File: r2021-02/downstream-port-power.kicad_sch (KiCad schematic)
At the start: 33 parts, among them J4 USB_A (female down), J5 USB_A_Stacked, J6 USB_A_Stacked, J7 USB_A_Stacked, U10 APL3511C, U11 NUP4202, U12 NUP4202, U13 NUP4202, U14 NUP4202, U15 NUP4202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

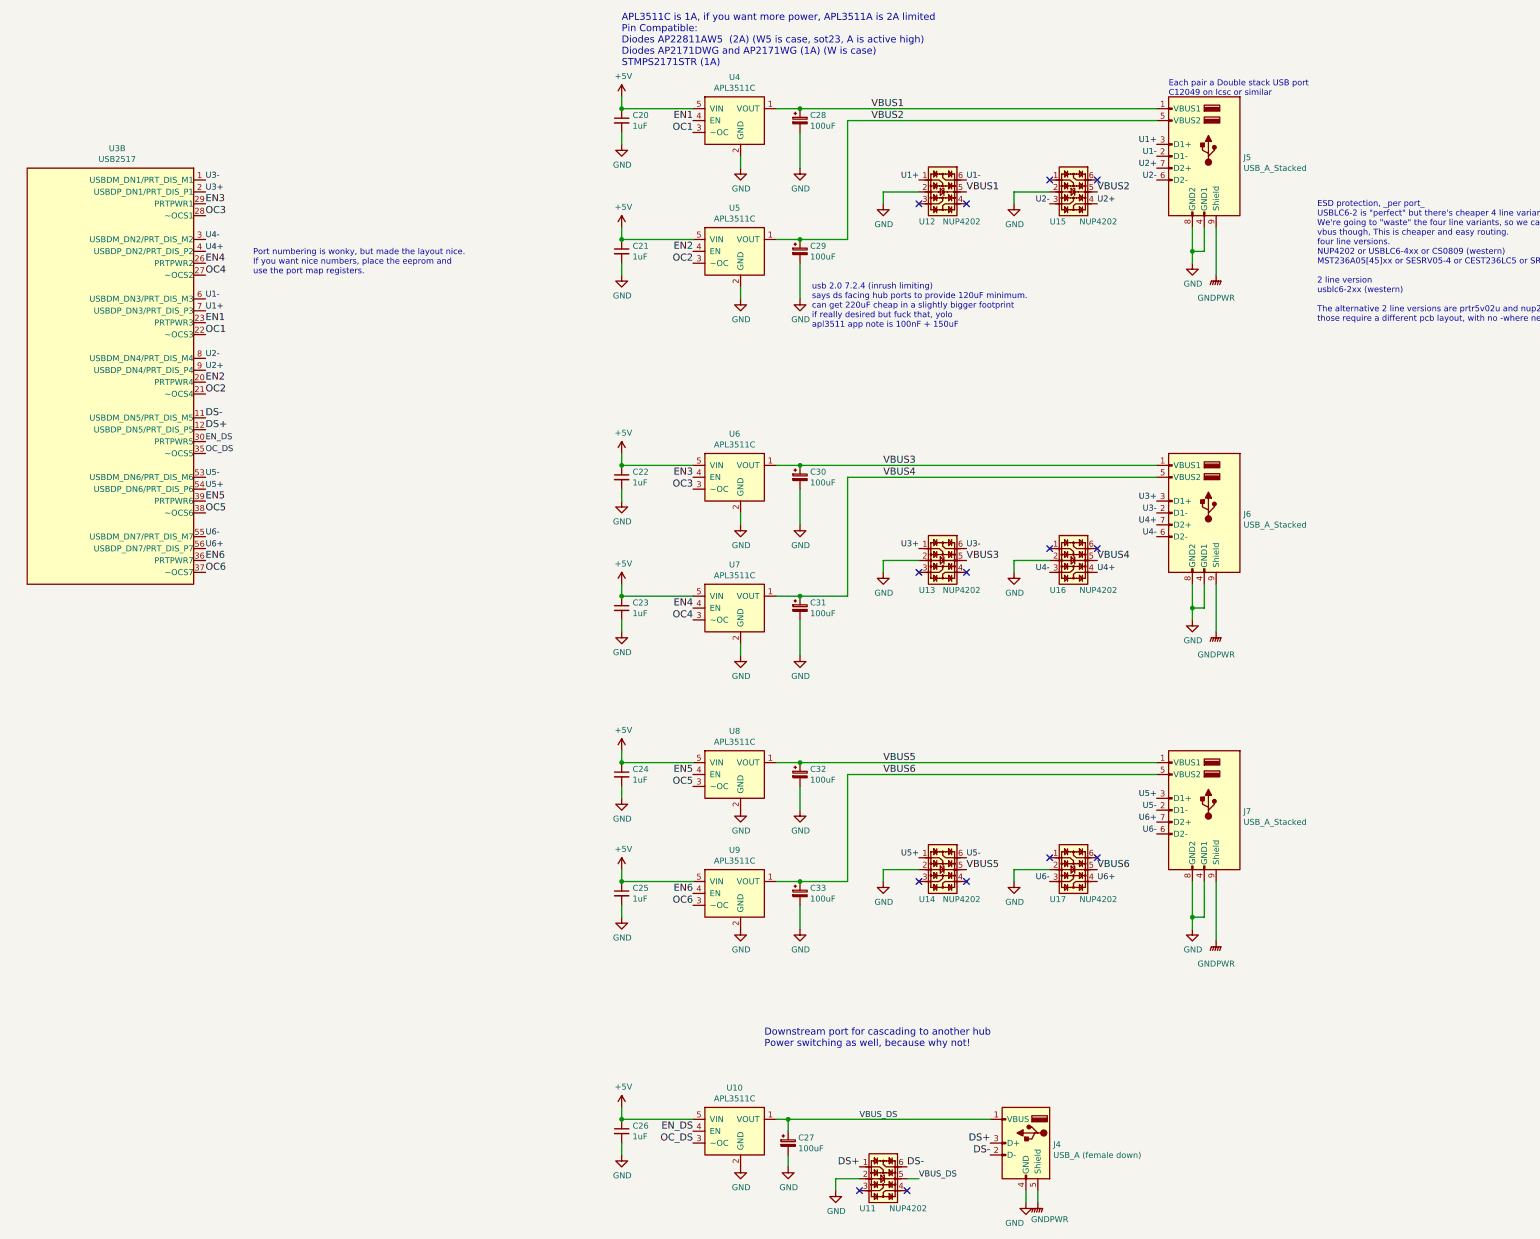
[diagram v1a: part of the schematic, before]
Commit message: BOM revisions for a rev3
Probably not going to bother even assembling rev2 pcbs.  Was missing
parts, found other things that were a little non-ideal.

Decided to start revising towards making it assembleable by JLC, so
using super cheap parts from their basic line where possible, and
minimizing bom items.
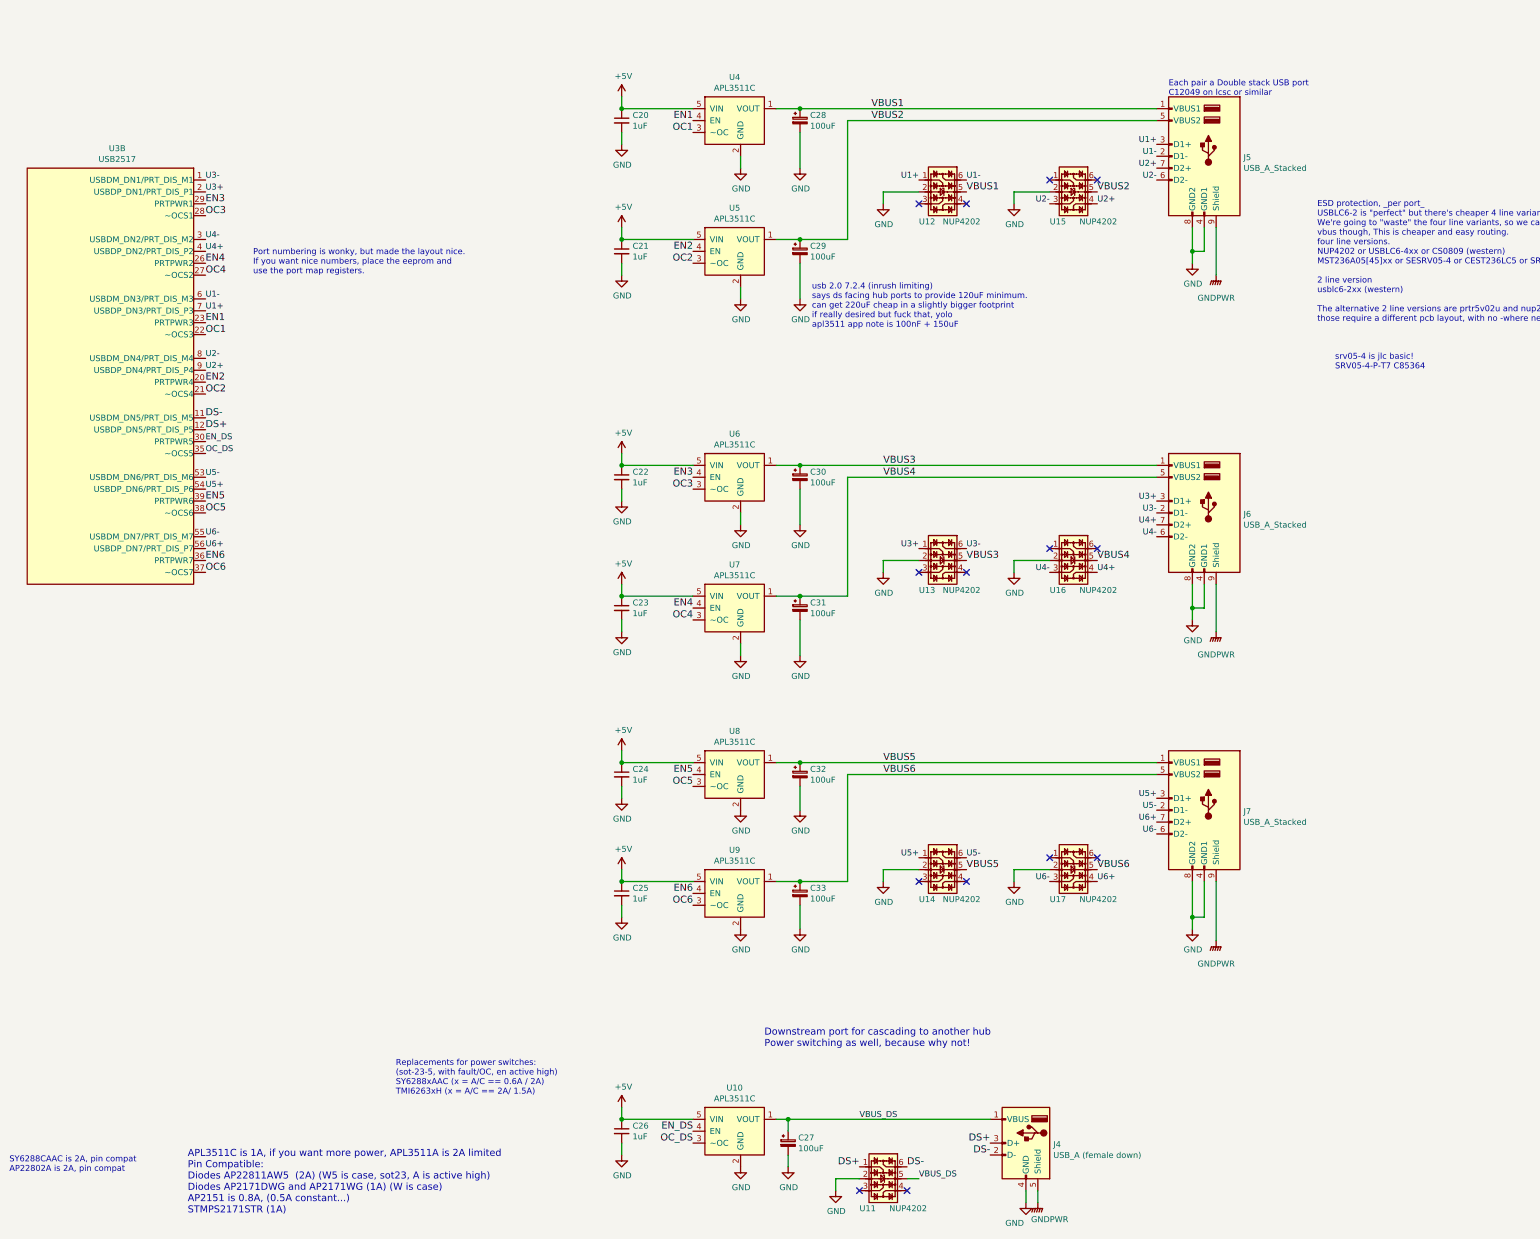
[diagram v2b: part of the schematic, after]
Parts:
- C20, C21, C22, C23, C24, C25, C26: MPN (none) -> CL10A105KB8NNNC; jlc-basic (none) -> 1; lcsc# (none) -> C15849
- C27, C28, C29, C30, C31, C32, C33: footprint Capacitor_SMD:CP_Elec_5x5.4 -> Capacitor_SMD:C_1206_3216Metric; MPN (none) -> CL31A107MQHNNNE; jlc-basic (none) -> 1; lcsc# (none) -> C15008
- U11, U12, U13, U14, U15, U16, U17: footprint Package_TO_SOT_SMD:SOT-363_SC-70-6 -> Package_TO_SOT_SMD:SOT-23-6; MPN (none) -> SRV05-4-P-T7; jlc-basic (none) -> 1; lcsc# (none) -> C85364
- U3: MPN (none) -> USB2517I-JZX-TR; jlc-basic (none) -> 0; lcsc# (none) -> C626667
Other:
- note added: "APL3511C is 1A, if you want more power, APL3511A is 2A limited Pin Compatible: Diodes AP22811AW5 (2A) (W5 is case, sot23, A is active high) Diodes AP2171DWG and AP2171WG (1A) (W is case) AP2151 is 0.8A, (0.5A constant...) STMPS2171STR (1A)"
- note added: "Replacements for power switches: (sot-23-5, with fault/OC, en active high) SY6288xAAC (x = A/C == 0.6A / 2A) TMI6263xH (x = A/C == 2A/ 1.5A)"
- note added: "SY6288CAAC is 2A, pin compat AP22802A is 2A, pin compat"
- note added: "srv05-4 is jlc basic! SRV05-4-P-T7 C85364"
- note removed: "APL3511C is 1A, if you want more power, APL3511A is 2A limited Pin Compatible: Diodes AP22811AW5 (2A) (W5 is case, sot23, A is active high) Diodes AP2171DWG and AP2171WG (1A) (W is case) STMPS2171STR (1A)"
